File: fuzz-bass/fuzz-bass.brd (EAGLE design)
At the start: 70 x 50 mm, 16 parts, among them Q1 2N4036, Q2 2N4036

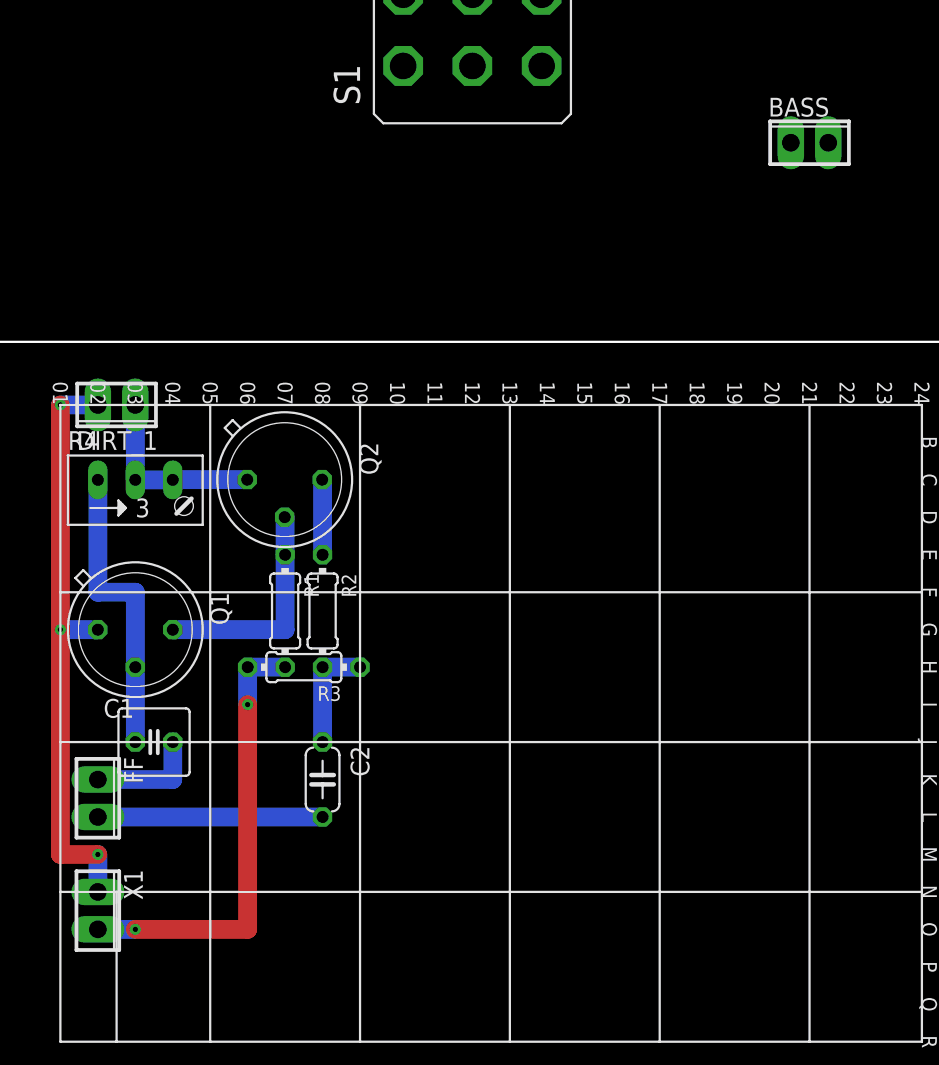
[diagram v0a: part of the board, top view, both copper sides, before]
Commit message: Add bass section to fuzz bass.
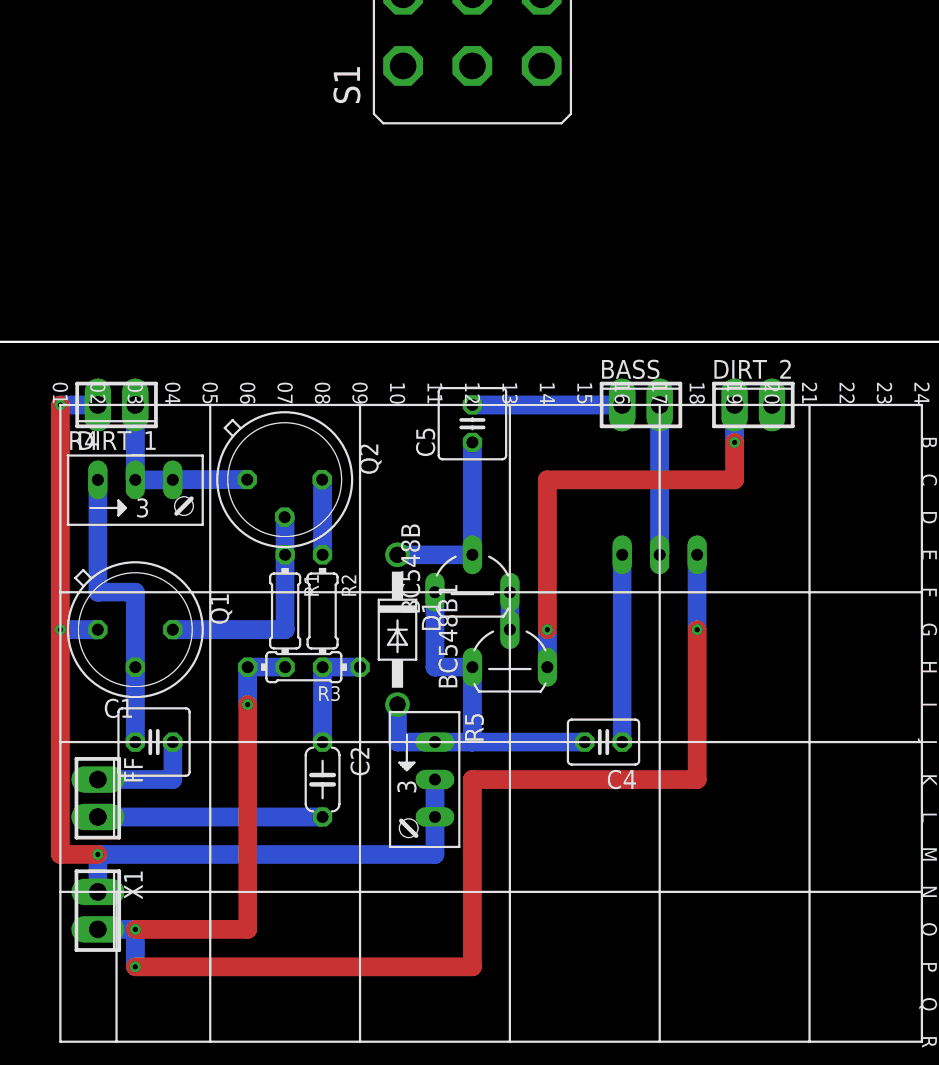
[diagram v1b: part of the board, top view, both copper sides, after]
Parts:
- added BC548B, BC548B1: (no value), transistor:TO92L
- added C4: 20u, rcl:C025-030X050
- added C5: 0.22u, adafruit:C025-050X050
- added D1: 1N4942, diode:DO41-10
- added DIRT_2: (no value), con-phoenix-254:2POL254
- added R5: 200k, pot:RJ9W
- added VOL_TRIM: 100k, pot:RJ9W
- moved BASS 21.1 mm to (47.0, 45.7)
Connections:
- new net BASS_DIRT_IN: BC548B1.1, DIRT.2-3, DIRT_2.1
- new net N$11: BC548B.2, C5.1, D1.C
- new net N$12: C4.1, VOL_TRIM.E
- new net N$7: BC548B.1, BC548B1.2
- new net N$8: BC548B.3, BC548B1.3, C4.2, D1.A, R5.E
- net +9V: now also R5.A, R5.S
- net BASS_IN: now also C5.2
- net BASS_OUT: now also VOL_TRIM.S
- net GND: now also DIRT.2-1, DIRT.2-2, VOL_TRIM.A
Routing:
- net GND: track 30.5 -> 99.1 mm, vias 2 -> 4
- net BASS_DIRT_IN: track 0.00 -> 30.5 mm, vias 0 -> 2
- net +9V: track 40.6 -> 68.6 mm
- net N$8: track 0.00 -> 27.9 mm
- net N$12: track 0.00 -> 12.7 mm
- net N$11: track 0.00 -> 12.7 mm
- net BASS_OUT: track 0.00 -> 10.2 mm
- net BASS_IN: track 0.00 -> 10.2 mm
- net N$7: track 0.00 -> 2.54 mm

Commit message: Updates to fuzz-bass.
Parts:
- added C6: 0.22u, rcl:C050-024X044
- added C7: 0.001u, rcl:C050-024X044
- added G1: AB9V, battery:AB9V
- added INPUT_JACK, OUTPUT_JACK1: JACK6.35MM, jack-eagle:JACK6.35MM
- added J1: (no value), con-jack:DCJ0303
- added LED1: (no value), led:LED3MM
- added R6: 100k, rcl:0204/7
- added R7: 1M, rcl:0204/7
- added S3: 3PDT, switch:3PDT
- added VOLUME1: 500k, pot:3RP/1610N
- moved DIRT 25.4 mm to (22.9, 129.5)
- moved S1 11.4 mm to (45.7, 76.2), turned to 0 degrees
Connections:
- net N$2 renamed FACE_DIRT_IN
- removed net FILTERED_INPUT: S1.2
- new net FUZZED_OUTPUT: S3.9, VOLUME.2
- new net INPUT: C7.1, INPUT_JACK.2, R7.2, S3.2, VOLUME1.1
- new net N$10: LED1.A, R6.2
- new net N$13: C6.1, VOLUME1.2, VOLUME1.3
- new net N$14: S3.1, S3.7
- new net N$15: G1.-, INPUT_JACK.1
- new net N$16: S1.5, VOLUME.3
- new net N$9: R6.1, S3.6
- new net TONE_INPUT: S3.3
- new net TONE_OUTPUT: C6.2, C7.2, S1.2
- net +9V: now also G1.+, S3.5
- net GND: now also INPUT_JACK.0, INPUT_JACK.3, LED1.K, OUTPUT_JACK1.0, OUTPUT_JACK1.3, R7.1
- net OUTPUT: now also OUTPUT_JACK1.2, S3.8; no longer S1.5
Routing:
- net TONE_OUTPUT: track 0.00 -> 71.2 mm
- net BASS_IN: track 10.2 -> 32.3 mm
- net BASS_OUT: track 10.2 -> 30.1 mm
- net INPUT: track 0.00 -> 11.0 mm
- net N$13: track 0.00 -> 7.62 mm
- net N$9: track 0.00 -> 6.13 mm
- net N$10: track 0.00 -> 2.54 mm
